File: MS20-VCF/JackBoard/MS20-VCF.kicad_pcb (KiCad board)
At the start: 2 copper layers, 40 x 121 mm, 33 parts, among them J11 Conn_JackBoard, J12 Conn_JackBoard, J13 FilterCV2, J14 FilterIn2, J15 FilterOut2, J3 Conn_JackBoard, J4 Conn_JackBoard, J6 FilterCV1, J7 FilterIn1, J8 FilterOut1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

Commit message: update ms20 + gerber
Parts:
- moved R36 14.2 mm to (75.0, 109.5), turned to 90 degrees
- moved R38 12.7 mm to (95.5, 101.8), turned to 270 degrees
- moved R17 10.0 mm to (109.0, 55.8), turned to 270 degrees
- moved R43 7.05 mm to (76.0, 127.0), turned to 90 degrees
- moved R42 7.01 mm to (109.5, 127.0), turned to 90 degrees
- moved CUTCV2 5.00 mm to (88.0, 130.0)
- moved J13 5.00 mm to (83.0, 133.0)
- moved J14 5.00 mm to (93.0, 133.0)
- moved J15 5.00 mm to (103.0, 133.0)
- moved Res2 5.00 mm to (103.0, 130.0)
- moved R39 4.51 mm to (109.5, 112.5)
- moved R15 4.36 mm to (80.0, 56.0)
- moved R21 4.36 mm to (95.8, 56.0)
- moved SW1 3.50 mm to (104.0, 43.0), turned to 180 degrees
- moved R22 3.29 mm to (75.5, 53.0)
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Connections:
- J11 pad 5: /Filtre2/FilterOut -> Net-(J11-Pad5)
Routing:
- net /Filtre2/Out1: track 35.2 -> 55.3 mm
- net /Filtre2/Cutoff: track 34.2 -> 53.2 mm, vias 0 -> 2
- net Net-(CUTOFF2-Pad2): track 9.15 -> 18.6 mm
- net /Filtre2/FilterOut: track 57.2 -> 48.3 mm
- net Net-(R42-Pad1): track 21.6 -> 13.0 mm
- net Net-(CUTOFF1-Pad3): track 22.3 -> 30.5 mm
- net +12V: track 85.7 -> 93.4 mm
- net /HPass: track 51.1 -> 57.8 mm
- net /Filtre2/LPass: track 45.0 -> 50.7 mm
- net /Out1: track 54.6 -> 49.2 mm
- net Net-(CUTCV2-Pad2): track 25.1 -> 20.8 mm
- net Net-(CUTCV1-Pad2): track 15.6 -> 11.6 mm
- net Net-(CUTOFF1-Pad2): track 7.04 -> 10.8 mm
- net /LPass: track 44.1 -> 47.4 mm
- net /Filtre2/HPass: track 55.1 -> 57.8 mm
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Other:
- board size 40 x 121 mm -> 40 x 110 mm

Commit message: Update gerber MS20-VCF
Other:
- net class Default removed
- net class Power removed

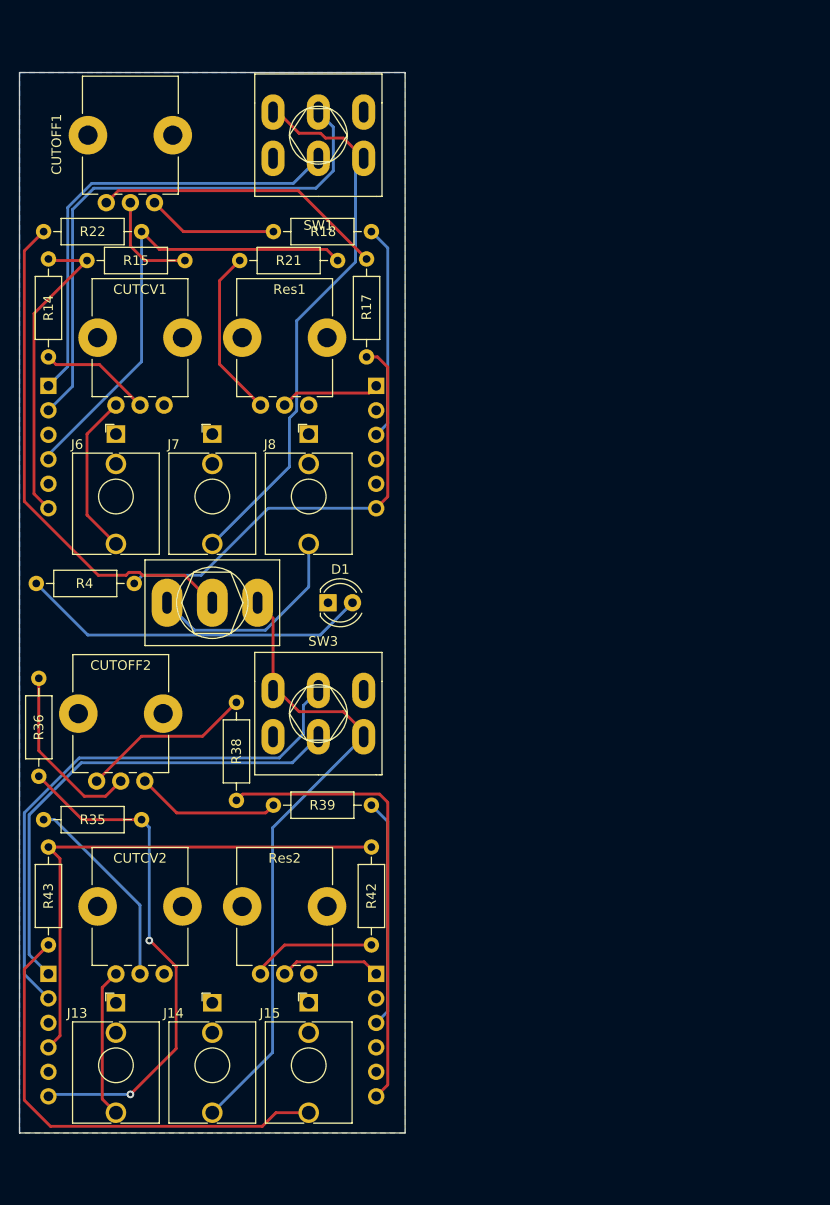
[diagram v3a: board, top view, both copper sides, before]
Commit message: update bom + gerber for jackboard
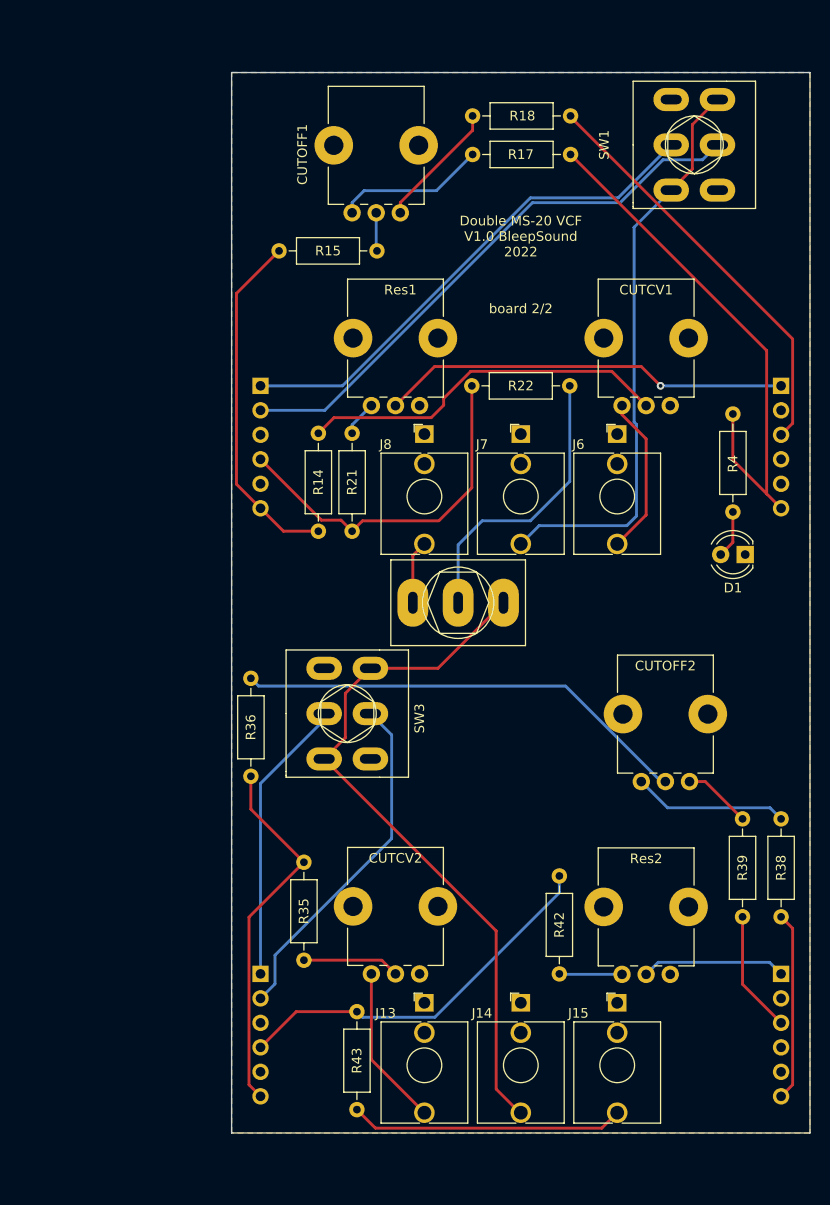
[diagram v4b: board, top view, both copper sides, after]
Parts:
- moved R4 64.5 mm to (147.0, 71.9), turned to -90 degrees
- moved R38 57.8 mm to (152.0, 113.9)
- moved R22 56.9 mm to (130.1, 69.0), turned to 180 degrees
- moved CUTOFF2 56.5 mm to (142.5, 110.0)
- moved CUTCV1 52.5 mm to (140.5, 71.0)
- moved J6 52.0 mm to (135.0, 74.0)
- moved D1 43.6 mm to (148.3, 86.5), turned to 180 degrees
- moved J12 42.0 mm to (152.0, 130.0)
- moved J4 42.0 mm to (152.0, 69.0)
- moved R39 40.2 mm to (148.0, 124.1), turned to 90 degrees
- moved R14 39.8 mm to (104.0, 84.1), turned to 90 degrees
- moved SW1 39.0 mm to (143.0, 44.0), turned to 90 degrees
- moved Res2 37.5 mm to (140.5, 130.1)
- moved R43 36.3 mm to (108.0, 144.1)
- moved J13 32.0 mm to (115.0, 133.0)
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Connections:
- J11 pad 3: Net-(J11-Pad3) -> unconnected-(J11-Pad3)
- J11 pad 5: Net-(J11-Pad5) -> unconnected-(J11-Pad5)
- J12 pad 2: Net-(J12-Pad2) -> unconnected-(J12-Pad2)
- J13 pad TN: Net-(J13-PadTN) -> unconnected-(J13-PadTN)
- J14 pad TN: Net-(J14-PadTN) -> unconnected-(J14-PadTN)
- J15 pad TN: Net-(J15-PadTN) -> unconnected-(J15-PadTN)
- J3 pad 3: Net-(J3-Pad3) -> unconnected-(J3-Pad3)
- J3 pad 5: Net-(J3-Pad5) -> unconnected-(J3-Pad5)
- J4 pad 2: Net-(J4-Pad2) -> unconnected-(J4-Pad2)
- J6 pad TN: Net-(J6-PadTN) -> unconnected-(J6-PadTN)
- J7 pad TN: Net-(J7-PadTN) -> unconnected-(J7-PadTN)
- J8 pad TN: Net-(J8-PadTN) -> unconnected-(J8-PadTN)
- SW1 pad 1: Net-(SW1-Pad1) -> unconnected-(SW1-Pad1)
- SW3 pad 1: Net-(SW3-Pad1) -> unconnected-(SW3-Pad1)
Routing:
- net /ResOut: track 10.3 -> 42.5 mm, vias 0 -> 1
- net Net-(D1-Pad2): track 36.4 -> 4.94 mm
- net Net-(CUTOFF2-Pad2): track 18.6 -> 47.4 mm
- net Net-(CUTCV1-Pad2): track 11.6 -> 38.5 mm
- net /FilterOut: track 52.9 -> 30.2 mm
- net /Filtre2/HPass: track 57.8 -> 36.1 mm
- net /Filtre2/LPass: track 50.7 -> 29.7 mm
- net /Filtre2/FilterOut: track 48.3 -> 28.5 mm
- net +12V: track 93.4 -> 75.2 mm
- net /JackOut: track 22.2 -> 6.60 mm
- net /Filtre2/Out1: track 55.3 -> 39.9 mm
- net /Filtre2/Cutoff: track 53.2 -> 38.3 mm, vias 2 -> 0
- net Net-(CUTOFF1-Pad3): track 30.5 -> 15.6 mm
- net Net-(R21-Pad1): track 17.6 -> 3.70 mm
- net /Out1: track 49.2 -> 37.5 mm
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- added copper zone on F.Cu, net GND
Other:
- board size 40 x 110 mm -> 60 x 110 mm
- board text added: "Double MS-20 VCF V1.0 BleepSound 2022"
- board text added: "board 2/2"

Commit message: fix jackboard and update gerber
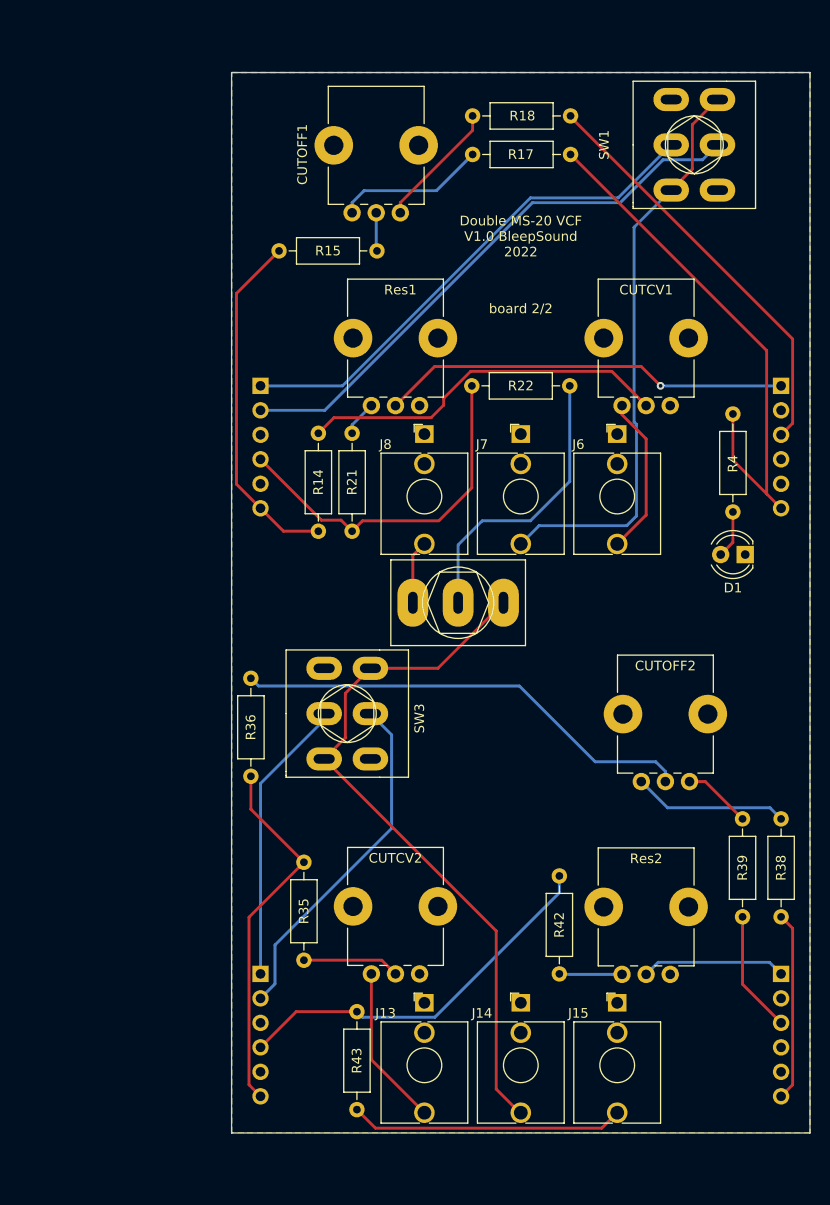
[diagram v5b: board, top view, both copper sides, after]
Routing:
- net Net-(CUTOFF2-Pad2): track 47.4 -> 48.1 mm
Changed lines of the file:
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@@
   )
   (segment (start 150.5 65.34) (end 150.5 80.2) (width 0.3) (layer "F.Cu") (net 2))
-  (segment (start 152.08 81.78) (end 152 81.7) (width 0.3) (layer "F.Cu") (net 2))
   (segment (start 150.5 80.2) (end 152 81.7) (width 0.3) (layer "F.Cu") (net 2))
   (segment (start 152 124.08) (end 153.199511 125.279511) (width 0.3) (layer "F.Cu") (net 2))
@@
   (segment (start 107.5 84.08) (end 106.350489 82.930489) (width 0.3) (layer "F.Cu") (net 5))
   (segment (start 119.92 79.58) (end 116.5 83) (width 0.3) (layer "F.Cu") (net 5))
-  (segment (start 99.5 131.04) (end 98 132.54) (width 0.3) (layer "B.Cu") (net 6))
-  (segment (start 99.5 128.059424) (end 99.5 131.04) (width 0.3) (layer "B.Cu") (net 6))
-  (segment (start 111.59952 115.959904) (end 99.5 128.059424) (width 0.3) (layer "B.Cu") (net 6))
+  (segment (start 99.5 131.04) (end 99.5 127) (width 0.3) (layer "B.Cu") (net 6))
+  (segment (start 98 132.54) (end 99.5 131.04) (width 0.3) (layer "B.Cu") (net 6))
+  (segment (start 111.59952 105.19952) (end 111.59952 114.90048) (width 0.3) (layer "B.Cu") (net 6))
   (segment (start 109.4 103) (end 111.59952 105.19952) (width 0.3) (layer "B.Cu") (net 6))
-  (segment (start 111.59952 105.19952) (end 111.59952 115.959904) (width 0.3) (layer "B.Cu") (net 6))
+  (segment (start 99.5 127) (end 111.59952 114.90048) (width 0.3) (layer "B.Cu") (net 6))
   (segment (start 108 133.92) (end 101.7 133.92) (width 0.3) (layer "F.Cu") (net 7))
   (segment (start 101.7 133.92) (end 98 137.62) (width 0.3) (layer "F.Cu") (net 7))
@@
   (segment (start 112.5 50) (end 112.5 51.05) (width 0.3) (layer "F.Cu") (net 12))
   (segment (start 120 42.5) (end 112.5 50) (width 0.3) (layer "F.Cu") (net 12))
-  (segment (start 110 54.92) (end 110.08 55) (width 0.3) (layer "F.Cu") (net 13))
   (segment (start 110 54.92) (end 110.08 55) (width 0.3) (layer "B.Cu") (net 13))
   (segment (start 110 51.05) (end 110 54.92) (width 0.3) (layer "B.Cu") (net 13))
@@
   (segment (start 144.13 110.05) (end 148 113.92) (width 0.3) (layer "F.Cu") (net 15))
   (segment (start 142.5 110.05) (end 144.13 110.05) (width 0.3) (layer "F.Cu") (net 15))
-  (segment (start 129.639999 100.139999) (end 139.55 110.05) (width 0.3) (layer "B.Cu") (net 16))
-  (segment (start 139.55 110.05) (end 140 110.05) (width 0.3) (layer "B.Cu") (net 16))
-  (segment (start 97.799999 100.139999) (end 129.639999 100.139999) (width 0.3) (layer "B.Cu") (net 16))
+  (segment (start 140 109) (end 139 108) (width 0.3) (layer "B.Cu") (net 16))
+  (segment (start 97.799999 100.139999) (end 124.860001 100.139999) (width 0.3) (layer "B.Cu") (net 16))
+  (segment (start 132.720002 108) (end 124.860001 100.139999) (width 0.3) (layer "B.Cu") (net 16))
+  (segment (start 140 110.05) (end 140 109) (width 0.3) (layer "B.Cu") (net 16))
   (segment (start 97 99.34) (end 97.799999 100.139999) (width 0.3) (layer "B.Cu") (net 16))
+  (segment (start 139 108) (end 132.720002 108) (width 0.3) (layer "B.Cu") (net 16))
   (segment (start 152 113.92) (end 150.850489 112.770489) (width 0.3) (layer "B.Cu") (net 17))
   (segment (start 140.220489 112.770489) (end 137.5 110.05) (width 0.3) (layer "B.Cu") (net 17))

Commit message: update ms20 gerbers
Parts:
- moved CUTCV2 26.0 mm to (140.5, 130.1)
- moved CUTCV1 26.0 mm to (114.5, 71.0)
- moved Res1 26.0 mm to (140.5, 71.0)
- moved Res2 26.0 mm to (114.5, 130.1)
- moved J13 20.0 mm to (135.0, 133.0)
- moved J6 20.0 mm to (115.0, 74.0)
- moved J8 20.0 mm to (135.0, 74.0)
- moved J14 10.0 mm to (115.0, 133.0)
- moved J15 10.0 mm to (125.0, 133.0)
- moved R42 1.00 mm to (130.0, 130.0), turned to 180 degrees
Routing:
- net Net-(CUTCV2-Pad2): track 10.1 -> 55.4 mm
- net Net-(R21-Pad1): track 3.70 -> 33.5 mm
- net Net-(CUTCV1-Pad2): track 38.5 -> 9.19 mm
- net /ResOut: track 42.5 -> 14.8 mm, vias 1 -> 0
- net /Filtre2/ResOut: track 15.0 -> 41.0 mm
- net /JackOut: track 6.60 -> 23.7 mm
- net Net-(R42-Pad1): track 6.52 -> 21.5 mm
- net /Filtre2/Out1: track 39.9 -> 25.9 mm
- net /Filtre2/FilterOut: track 28.5 -> 18.4 mm
- net Filter2In: track 73.2 -> 69.0 mm
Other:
- board text added: "12HP"
